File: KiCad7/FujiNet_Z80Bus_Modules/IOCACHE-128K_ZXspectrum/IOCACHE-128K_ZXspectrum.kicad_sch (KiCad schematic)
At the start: 4 parts, among them IC4 74HC590N

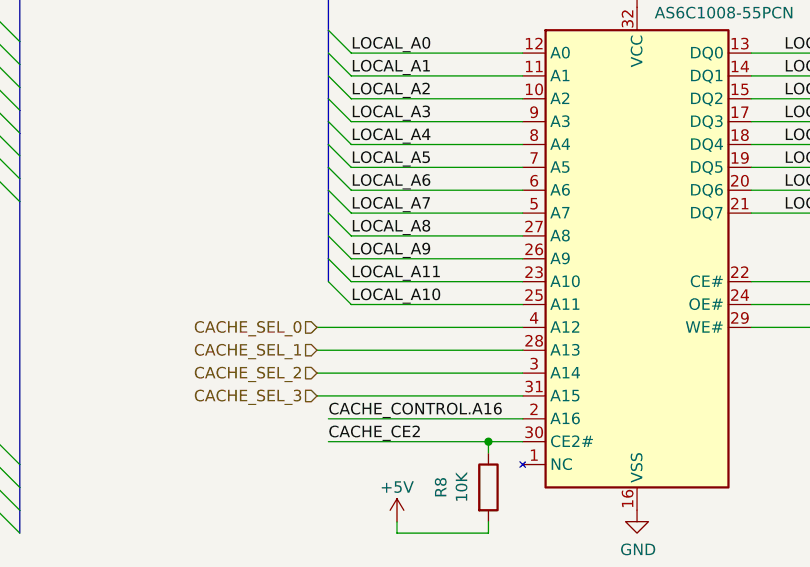
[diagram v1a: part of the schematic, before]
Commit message: Fixed a bug A11 A10 mixed up on CACHE IC
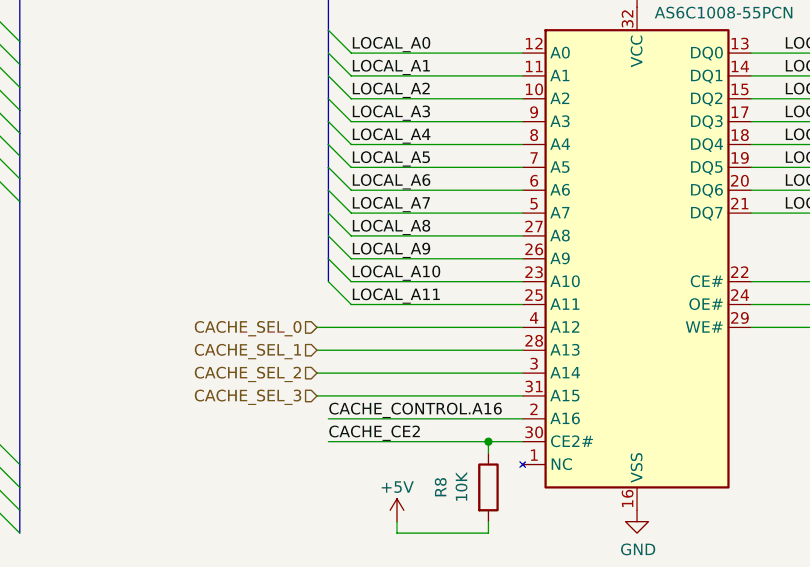
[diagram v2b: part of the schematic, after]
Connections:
- net LOCAL_A10: now also CACHE1.23 (A10); no longer CACHE1.25 (A11)
- net LOCAL_A11: now also CACHE1.25 (A11); no longer CACHE1.23 (A10)
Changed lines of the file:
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@@
     (effects (font (size 1.27 1.27)) (justify left bottom))
   )
-  (label "LOCAL_A11" (at 182.88 86.36 0) (fields_autoplaced)
+  (label "LOCAL_A11" (at 182.88 88.9 0) (fields_autoplaced)
     (effects (font (size 1.27 1.27)) (justify left bottom))
   )
@@
     (effects (font (size 1.27 1.27)) (justify left bottom))
   )
-  (label "LOCAL_A10" (at 182.88 88.9 0) (fields_autoplaced)
+  (label "LOCAL_A10" (at 182.88 86.36 0) (fields_autoplaced)
     (effects (font (size 1.27 1.27)) (justify left bottom))
   )

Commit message: KiCad IOCACHE_impl
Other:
- added sheet IOCACHE-128K_ZXspectrum_connectors (IOCACHE-128K_ZXspectrum_connectors.kicad_sch)

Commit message: Narrow versions of RIO CACHE
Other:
- removed sheet IOCACHE-128K_ZXspectrum_connectors
